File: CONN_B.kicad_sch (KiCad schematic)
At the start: 4 parts, among them J2 USB_B, J5 6437288-4, J7 Conn_ARM_SWD_TagConnect_TC2030

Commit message: lsd circuit in place
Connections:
- net +3V3 renamed 3V3
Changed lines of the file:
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@@
 			)
 		)
-		(property "Value" "+3V3"
+		(property "Value" "3V3"
 			(at 26.416 20.066 0)
 			(effects
@@
 			)
 		)
-		(property "Value" "+3V3"
+		(property "Value" "3V3"
 			(at 180.086 46.736 0)
 			(effects

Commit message: added 3.3v gpio input protection
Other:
- moved on the sheet: C51, J2, J5, J7

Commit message: working on mcu layout
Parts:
- added R86, R87, R88, R89: 47R, Resistor_SMD:R_0603_1608Metric_Pad0.98x0.95mm_HandSolder, symbol Device:R
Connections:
- net STM_NRST: now also R86.1; no longer J5.19, J7.3 (~{RESET})
- net STM_SWDCLK: now also R88.1; no longer J5.17, J7.4 (SWCLK)
- net STM_SWDIO: now also R89.1; no longer J5.16, J7.2 (SWDIO)
- net STM_SWO: now also R87.1; no longer J5.18, J7.6 (SWO)
- new net: J5.16, J7.2 (SWDIO), R89.2
- new net: J5.19, J7.3 (~{RESET}), R86.2
- new net: J5.17, J7.4 (SWCLK), R88.2
- new net: J5.18, J7.6 (SWO), R87.2
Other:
- moved on the sheet: C51, J2, J5, J7

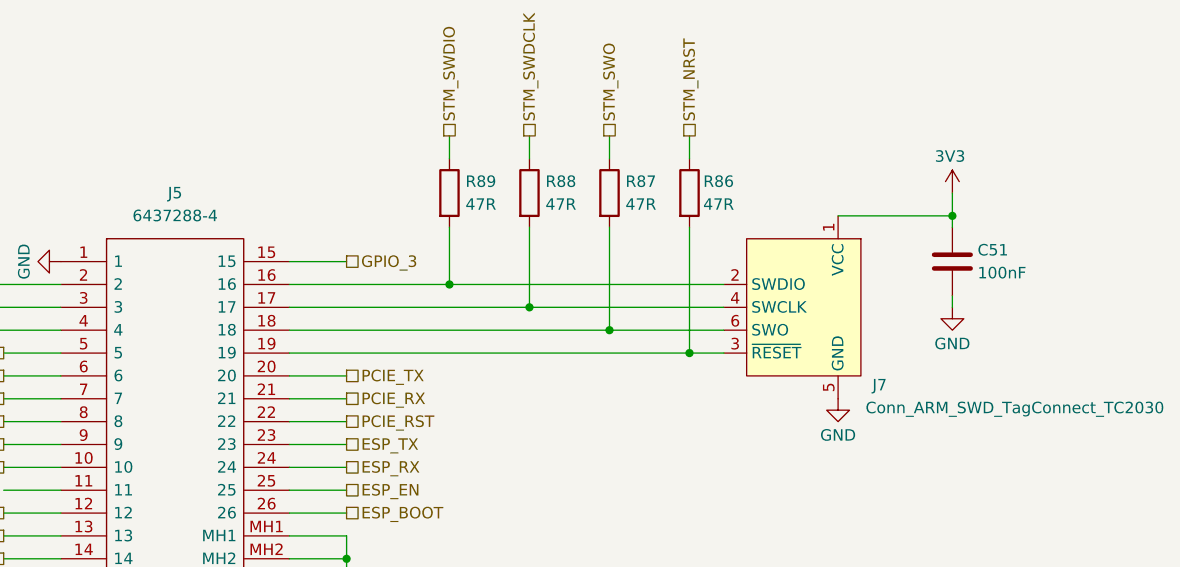
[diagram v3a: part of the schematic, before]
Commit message: redid annotations, added test point
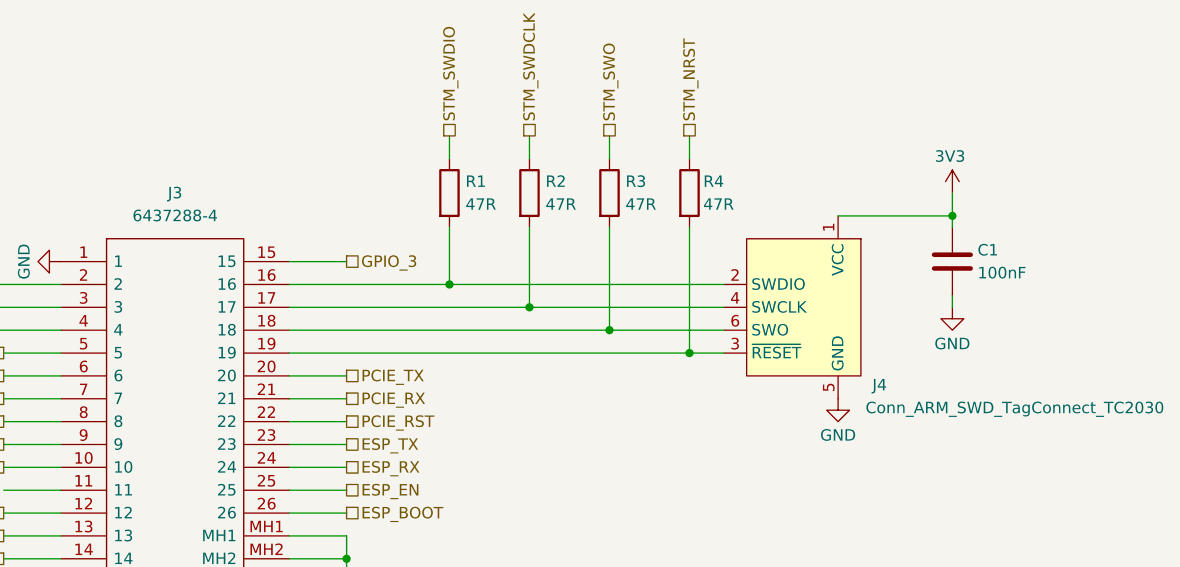
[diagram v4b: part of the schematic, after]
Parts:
- renumbered C51 to C1, J5 to J3, J7 to J4, R89 to R1, R88 to R2, R87 to R3, R86 to R4
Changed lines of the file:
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@@
 		(on_board yes)
 		(dnp no)
-		(property "Reference" "C51"
+		(property "Reference" "C1"
 			(at 184.404 49.53 0)
 			(effects
@@
 			(project "NCU"
 				(path "/3aee14c3-5480-4f7c-989e-3fef81779034/58530478-b11f-47ae-90e9-56fd185c9f38"
-					(reference "C51")
+					(reference "C1")
 					(unit 1)
 				)
@@
 		(on_board yes)
 		(dnp no)
-		(property "Reference" "#PWR086"
+		(property "Reference" "#PWR046"
 			(at 76.2 50.8 0)
 			(effects
@@
 			(project "NCU"
 				(path "/3aee14c3-5480-4f7c-989e-3fef81779034/58530478-b11f-47ae-90e9-56fd185c9f38"
-					(reference "#PWR086")
+					(reference "#PWR046")
 					(unit 1)
 				)
@@
 		(on_board yes)
 		(dnp no)
-		(property "Reference" "R89"
+		(property "Reference" "R1"
 			(at 127.508 41.91 0)
 			(effects
@@
 			(project "NCU"
 				(path "/3aee14c3-5480-4f7c-989e-3fef81779034/58530478-b11f-47ae-90e9-56fd185c9f38"
-					(reference "R89")
+					(reference "R1")
 					(unit 1)
 				)
@@
 		(on_board yes)
 		(dnp no)
-		(property "Reference" "#PWR091"
+		(property "Reference" "#PWR043"
 			(at 20.32 24.13 0)
 			(effects
@@
 			(project "NCU"
 				(path "/3aee14c3-5480-4f7c-989e-3fef81779034/58530478-b11f-47ae-90e9-56fd185c9f38"
-					(reference "#PWR091")
+					(reference "#PWR043")
 					(unit 1)
 				)
@@
 		(on_board yes)
 		(dnp no)
-		(property "Reference" "J7"
+		(property "Reference" "J4"
 			(at 172.72 64.516 0)
 			(effects
@@
 			(project "NCU"
 				(path "/3aee14c3-5480-4f7c-989e-3fef81779034/58530478-b11f-47ae-90e9-56fd185c9f38"
-					(reference "J7")
+					(reference "J4")
 					(unit 1)
 				)
@@
 		(on_board yes)
 		(dnp no)
-		(property "Reference" "#PWR04"
+		(property "Reference" "#PWR045"
 			(at 45.72 73.66 0)
 			(effects
@@
 			(project "NCU"
 				(path "/3aee14c3-5480-4f7c-989e-3fef81779034/58530478-b11f-47ae-90e9-56fd185c9f38"
-					(reference "#PWR04")
+					(reference "#PWR045")
 					(unit 1)
 				)
@@
 		(on_board yes)
 		(dnp no)
-		(property "Reference" "#PWR097"
+		(property "Reference" "#PWR044"
 			(at 20.32 31.75 0)
 			(effects
@@
 			(project "NCU"
 				(path "/3aee14c3-5480-4f7c-989e-3fef81779034/58530478-b11f-47ae-90e9-56fd185c9f38"
-					(reference "#PWR097")
+					(reference "#PWR044")
 					(unit 1)
 				)
@@
 		(on_board yes)
 		(dnp no)
-		(property "Reference" "R87"
+		(property "Reference" "R3"
 			(at 145.288 41.91 0)
 			(effects
@@
 			(project "NCU"
 				(path "/3aee14c3-5480-4f7c-989e-3fef81779034/58530478-b11f-47ae-90e9-56fd185c9f38"
-					(reference "R87")
+					(reference "R3")
 					(unit 1)
 				)
@@
 		(on_board yes)
 		(dnp no)
-		(property "Reference" "#PWR094"
+		(property "Reference" "#PWR048"
 			(at 168.91 72.39 0)
 			(effects
@@
 			(project "NCU"
 				(path "/3aee14c3-5480-4f7c-989e-3fef81779034/58530478-b11f-47ae-90e9-56fd185c9f38"
-					(reference "#PWR094")
+					(reference "#PWR048")
 					(unit 1)
 				)
@@
 		(on_board yes)
 		(dnp no)
-		(property "Reference" "R88"
+		(property "Reference" "R2"
 			(at 136.398 41.91 0)
 			(effects
@@
 			(project "NCU"
 				(path "/3aee14c3-5480-4f7c-989e-3fef81779034/58530478-b11f-47ae-90e9-56fd185c9f38"
-					(reference "R88")
+					(reference "R2")
 					(unit 1)
 				)
@@
 		(on_board yes)
 		(dnp no)
-		(property "Reference" "R86"
+		(property "Reference" "R4"
 			(at 153.924 41.91 0)
 			(effects
@@
 			(project ""
 				(path "/3aee14c3-5480-4f7c-989e-3fef81779034/58530478-b11f-47ae-90e9-56fd185c9f38"
-					(reference "R86")
+					(reference "R4")
 					(unit 1)
 				)
@@
 		(on_board yes)
 		(dnp no)
-		(property "Reference" "#PWR096"
+		(property "Reference" "#PWR049"
 			(at 181.61 46.99 0)
 			(effects
@@
 			(project "NCU"
 				(path "/3aee14c3-5480-4f7c-989e-3fef81779034/58530478-b11f-47ae-90e9-56fd185c9f38"
-					(reference "#PWR096")
+					(reference "#PWR049")
 					(unit 1)
 				)
@@
 		(on_board yes)
 		(dnp no)
-		(property "Reference" "#PWR087"
+		(property "Reference" "#PWR047"
 			(at 114.3 91.44 0)
 			(effects
@@
 			(project "NCU"
 				(path "/3aee14c3-5480-4f7c-989e-3fef81779034/58530478-b11f-47ae-90e9-56fd185c9f38"
-					(reference "#PWR087")
+					(reference "#PWR047")
 					(unit 1)
 				)
@@
 		(dnp no)
 		(fields_autoplaced yes)
-		(property "Reference" "J5"
+		(property "Reference" "J3"
 			(at 95.25 43.18 0)
 			(effects
@@
 			(project "NCU"
 				(path "/3aee14c3-5480-4f7c-989e-3fef81779034/58530478-b11f-47ae-90e9-56fd185c9f38"
-					(reference "J5")
+					(reference "J3")
 					(unit 1)
 				)
@@
 		(on_board yes)
 		(dnp no)
-		(property "Reference" "#PWR095"
+		(property "Reference" "#PWR050"
 			(at 181.61 62.23 0)
 			(effects
@@
 			(project "NCU"
 				(path "/3aee14c3-5480-4f7c-989e-3fef81779034/58530478-b11f-47ae-90e9-56fd185c9f38"
-					(reference "#PWR095")
-					(unit 1)
-				)
+					(reference "#PWR050")
+					(unit 1)
+				)
